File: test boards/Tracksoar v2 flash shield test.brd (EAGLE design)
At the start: 44.2 x 19.6 mm, 3 parts

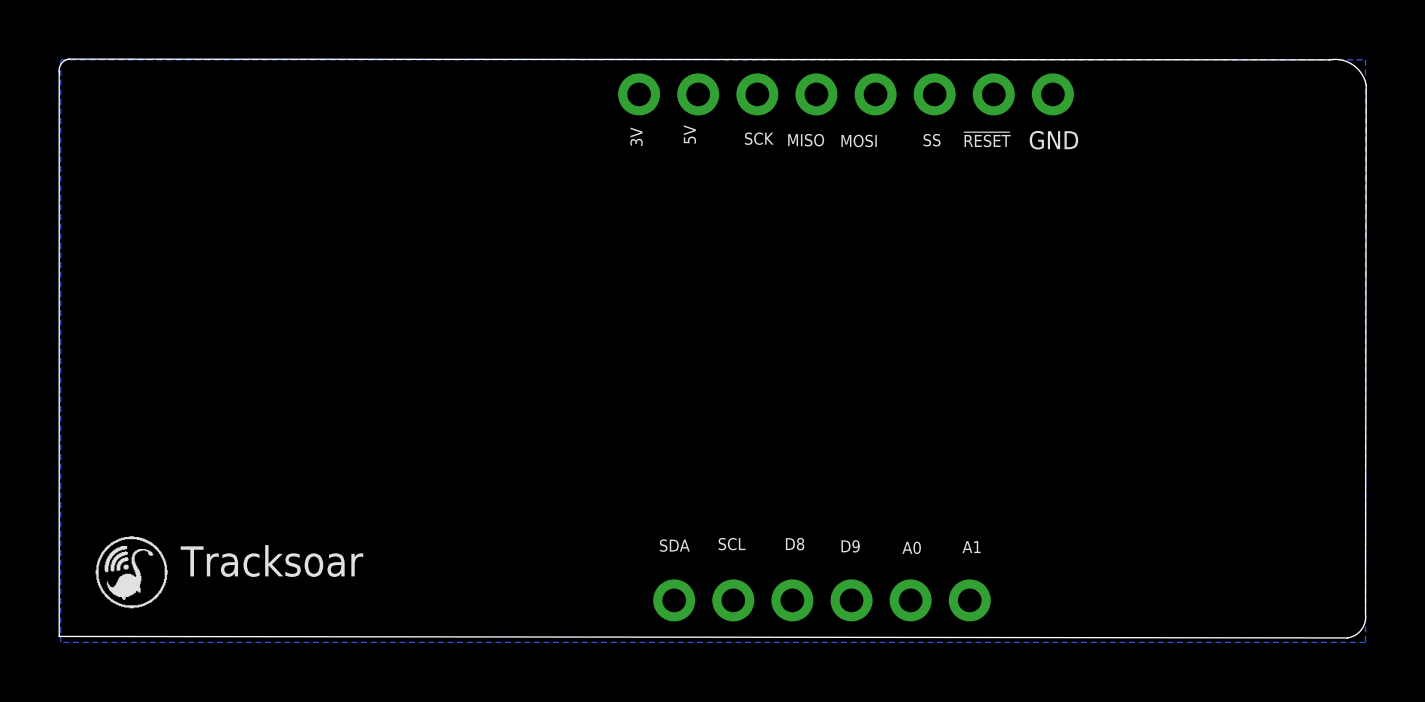
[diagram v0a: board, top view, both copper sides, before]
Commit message: Added boards
Added boards for a cutdown circuit, spi flash storage and spi flash breakout board and a shield template.
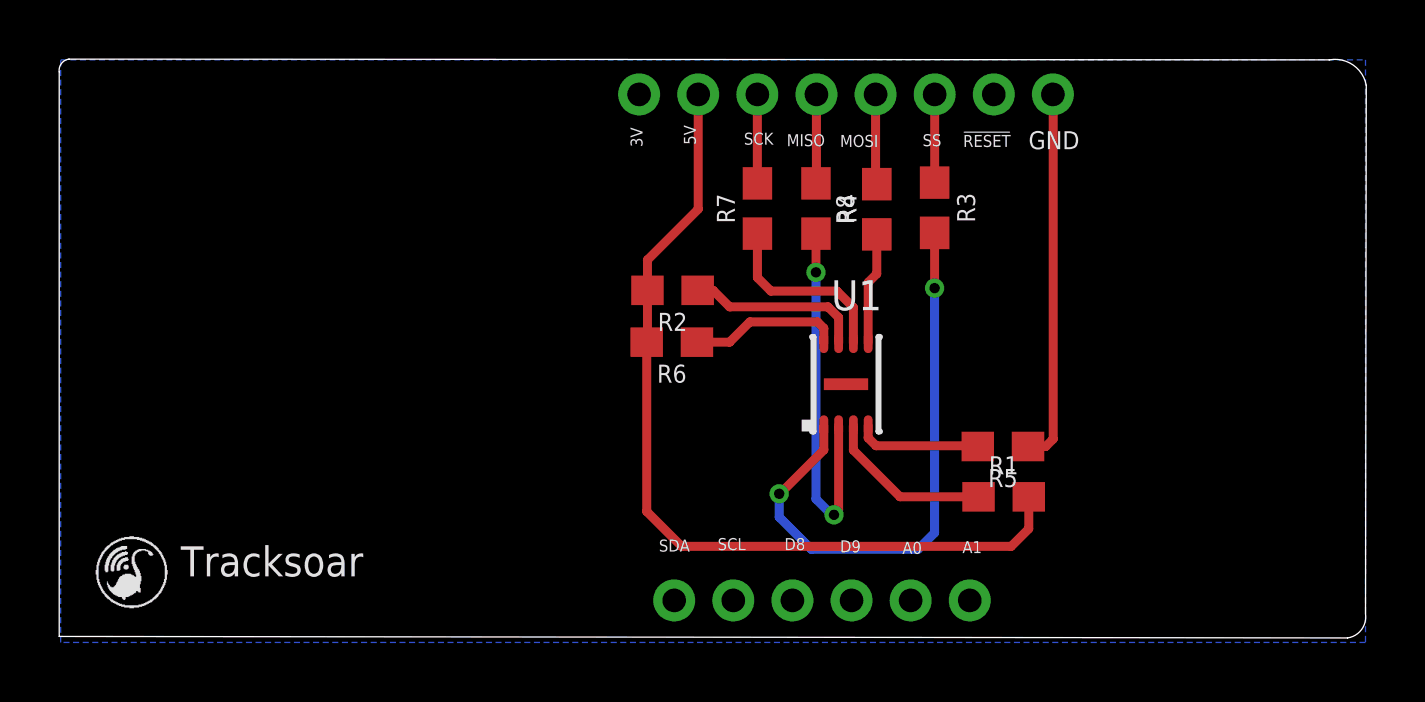
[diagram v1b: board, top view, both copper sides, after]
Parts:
- added R1, R2: 10k, SparkFun-Resistors:0603
- added R3, R4, R5, R6, R7, R8: (no value), SparkFun-Resistors:0603
- added U1: W25X20CLUX, memory-winbond:SON-8-50P-300W-200L-100H-40F-20EW-165EL
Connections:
- new net N$1: R1.1, U1.3
- new net N$12: R8.1, U1.5
- new net N$2: R2.1, U1.7
- new net N$3: R3.2, U1.1
- new net N$6: R4.2, U1.2
- new net N$7: R5.2, U1.4
- new net N$8: R6.1, U1.8
- new net N$9: R7.1, U1.6
- net GND: now also R5.1
- net MISO: now also R4.1
- net MOSI: now also R8.2
- net SCK: now also R7.2
- net SS: now also R3.1
- net VCC: now also R1.2, R2.2, R6.2
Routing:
- net VCC: track 0.00 -> 29.6 mm
- net N$3: track 0.00 -> 19.8 mm, vias 0 -> 2
- net N$6: track 0.00 -> 12.9 mm, vias 0 -> 2
- net GND: track 0.00 -> 12.6 mm
- net N$9: track 0.00 -> 6.35 mm
- net N$2: track 0.00 -> 6.00 mm
- net N$1: track 0.00 -> 5.72 mm
- net N$8: track 0.00 -> 5.16 mm
- net N$7: track 0.00 -> 4.25 mm
- net N$12: track 0.00 -> 3.79 mm
- net MOSI: track 0.00 -> 3.05 mm
- net MISO: track 0.00 -> 3.02 mm
- net SCK: track 0.00 -> 3.01 mm
- net SS: track 0.00 -> 2.99 mm
